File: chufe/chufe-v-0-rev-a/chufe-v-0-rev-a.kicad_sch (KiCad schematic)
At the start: 0 parts

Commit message: agregar borrador
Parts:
- added C1: 100n, symbol Device:C
- added C2: C, symbol Device:C
- added C3: 22u, symbol Device:C_Polarized
- added D1: D, symbol Device:D
- added D2, D3: LED, symbol Device:LED
- added J1: Barrel_Jack_Switch, Connector_BarrelJack:BarrelJack_Horizontal, symbol Connector:Barrel_Jack_Switch
- added R1, R2: 1k, symbol Device:R
- added U1: L7805, symbol Regulator_Linear:L7805
- added U2: URA2412YMD-20WR3_C5369773, easyeda2kicad:PWRM-TH_YLPTEC_VRBXXXXYMD-20WR3, symbol easyeda2kicad:URA2412YMD-20WR3_C5369773
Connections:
- new net: D1.2 (A), D2.2 (A), J1.1
- new net: D3.1 (K), R2.1
- new net: C1.1, D1.1 (K), U1.1 (IN), U2.2 (+VIN)
- new net: D2.1 (K), R1.1
- new net: C2.1, U1.2 (GND)
- new net +12V: U2.3 (+VO1)
- new net +5V: C3.1, D3.2 (A), U1.3 (OUT)
- new net -12V: U2.5 (-VO2)
- new net GND: C1.2, C2.2, C3.2, J1.2, J1.3, R1.2, R2.2, U2.1 (-VIN), U2.4 (COM)
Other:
- company: (none) -> piruetas SpA

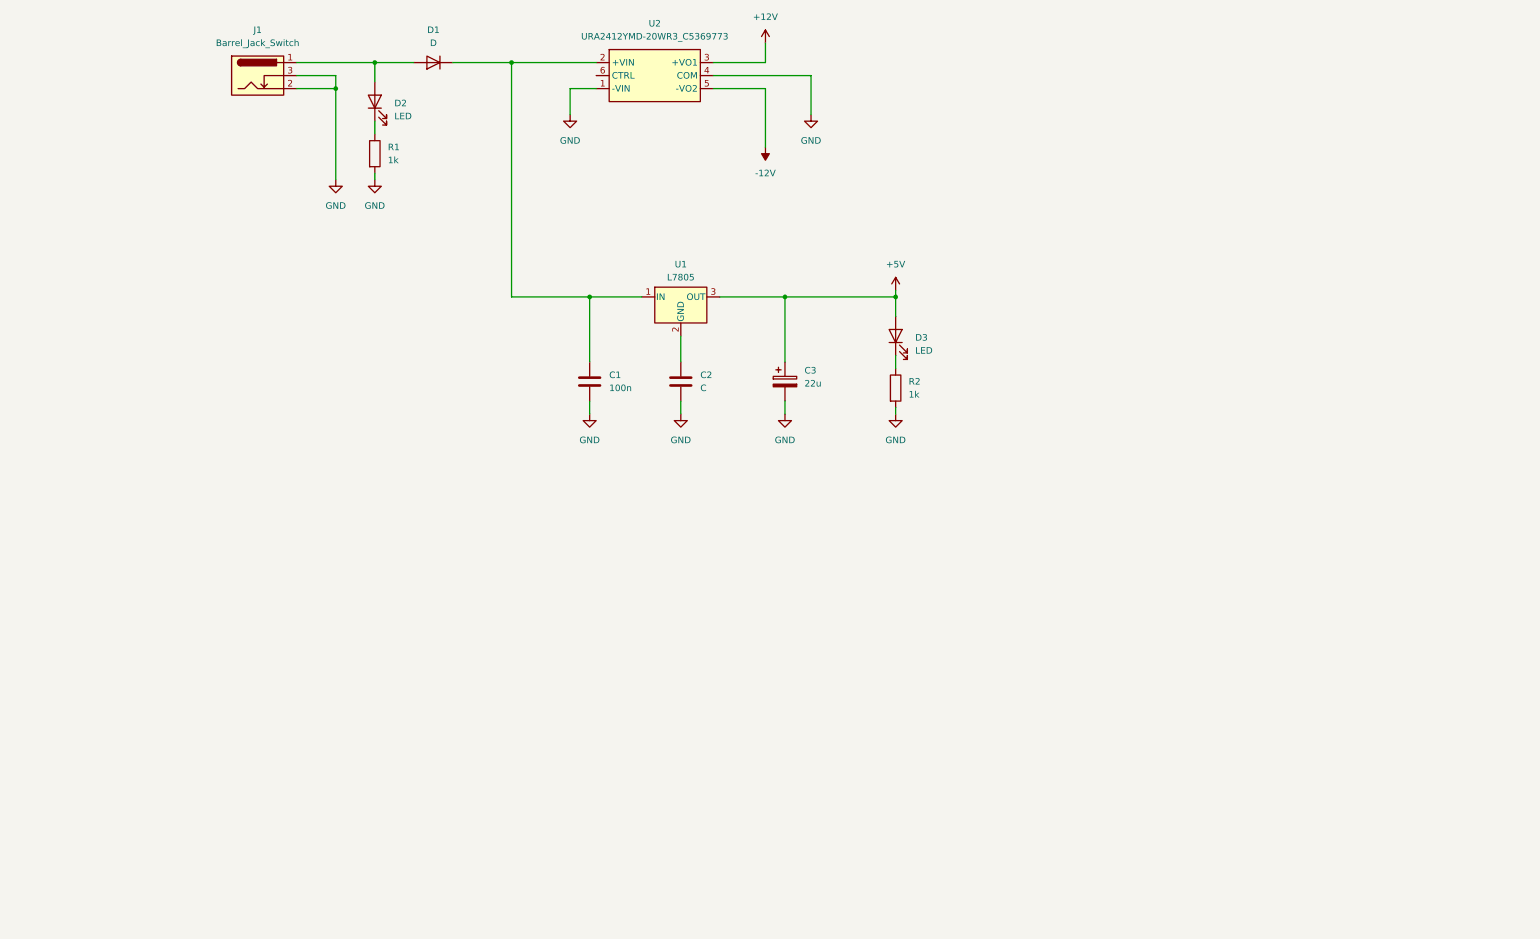
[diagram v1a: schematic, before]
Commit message: agregar ocho conectores
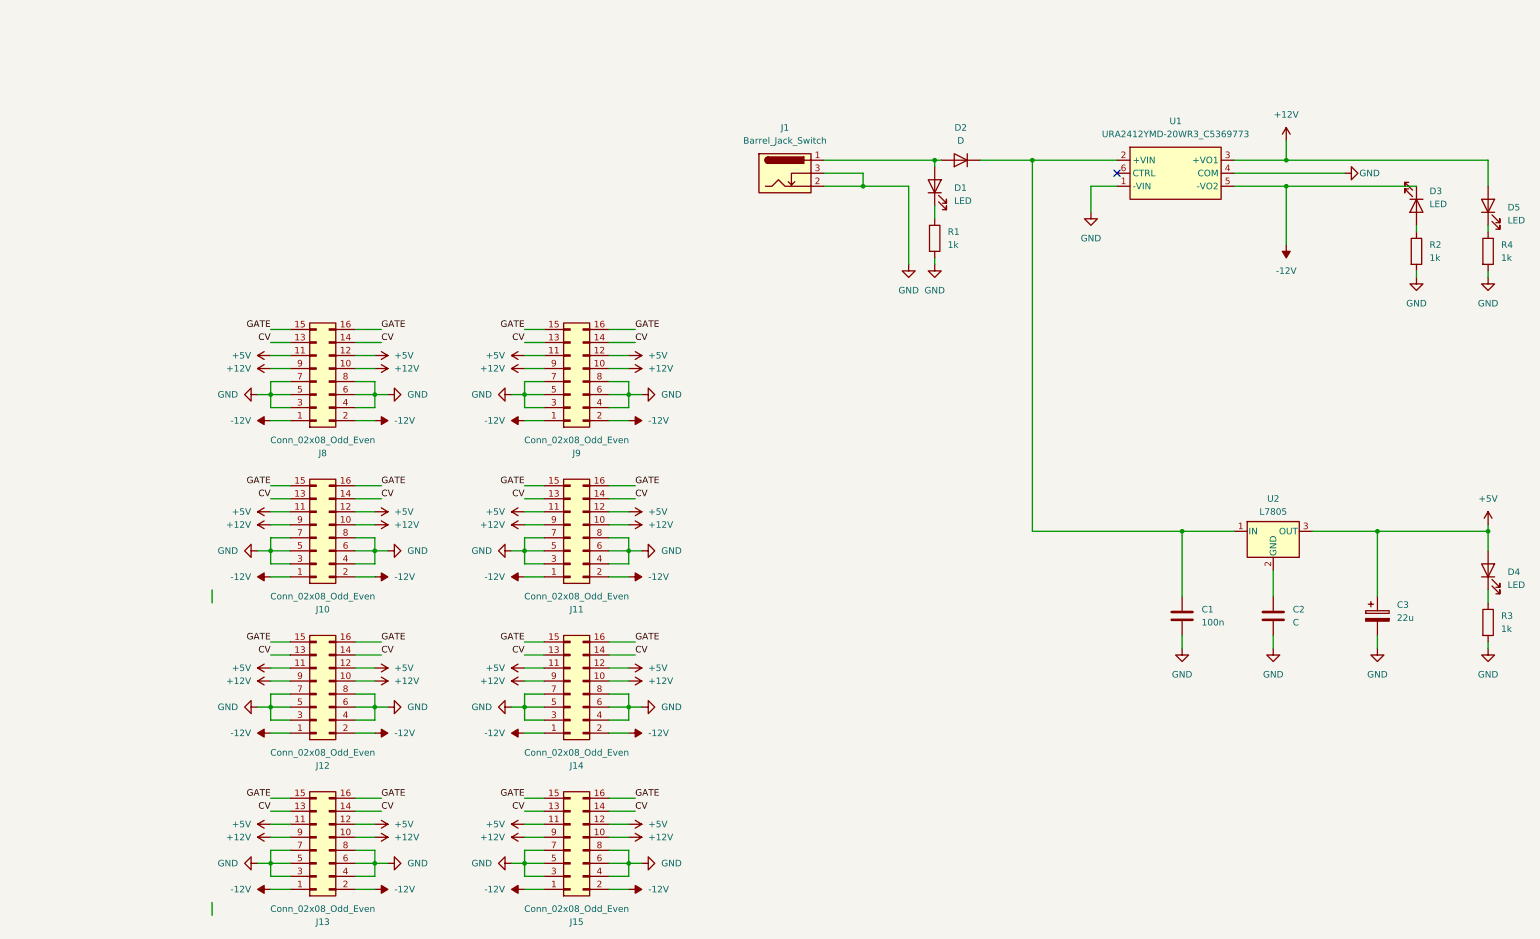
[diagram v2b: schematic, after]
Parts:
- removed D1: D, symbol Device:D
- removed D2: LED, symbol Device:LED
- removed U1: L7805, symbol Regulator_Linear:L7805
- removed U2: URA2412YMD-20WR3_C5369773, easyeda2kicad:PWRM-TH_YLPTEC_VRBXXXXYMD-20WR3, symbol easyeda2kicad:URA2412YMD-20WR3_C5369773
- added D1, D4, D5: LED, symbol Device:LED
- added D2: D, symbol Device:D
- added J10, J11, J12, J13, J14, J15, J8, J9: Conn_02x08_Odd_Even, symbol Connector_Generic:Conn_02x08_Odd_Even
- added R3, R4: 1k, symbol Device:R
- added U1: URA2412YMD-20WR3_C5369773, easyeda2kicad:PWRM-TH_YLPTEC_VRBXXXXYMD-20WR3, symbol easyeda2kicad:URA2412YMD-20WR3_C5369773
- added U2: L7805, symbol Regulator_Linear:L7805
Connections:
- net +12V: now also D5.2 (A), J10.10 (Pin_10), J10.9 (Pin_9), J11.10 (Pin_10), J11.9 (Pin_9), J12.10 (Pin_10), J12.9 (Pin_9), J13.10 (Pin_10), J13.9 (Pin_9), J14.10 (Pin_10), J14.9 (Pin_9), J15.10 (Pin_10), J15.9 (Pin_9), J8.10 (Pin_10), J8.9 (Pin_9), J9.10 (Pin_10), J9.9 (Pin_9), U1.3 (+VO1)
- net +5V: now also D4.2 (A), J10.11 (Pin_11), J10.12 (Pin_12), J11.11 (Pin_11), J11.12 (Pin_12), J12.11 (Pin_11), J12.12 (Pin_12), J13.11 (Pin_11), J13.12 (Pin_12), J14.11 (Pin_11), J14.12 (Pin_12), J15.11 (Pin_11), J15.12 (Pin_12), J8.11 (Pin_11), J8.12 (Pin_12), J9.11 (Pin_11), J9.12 (Pin_12), U2.3 (OUT); no longer D3.2 (A)
- net -12V: now also D3.1 (K), J10.1 (Pin_1), J10.2 (Pin_2), J11.1 (Pin_1), J11.2 (Pin_2), J12.1 (Pin_1), J12.2 (Pin_2), J13.1 (Pin_1), J13.2 (Pin_2), J14.1 (Pin_1), J14.2 (Pin_2), J15.1 (Pin_1), J15.2 (Pin_2), J8.1 (Pin_1), J8.2 (Pin_2), J9.1 (Pin_1), J9.2 (Pin_2), U1.5 (-VO2)
- net GND: now also J10.3 (Pin_3), J10.4 (Pin_4), J10.5 (Pin_5), J10.6 (Pin_6), J10.7 (Pin_7), J10.8 (Pin_8), J11.3 (Pin_3), J11.4 (Pin_4), J11.5 (Pin_5), J11.6 (Pin_6), J11.7 (Pin_7), J11.8 (Pin_8), J12.3 (Pin_3), J12.4 (Pin_4), J12.5 (Pin_5), J12.6 (Pin_6), J12.7 (Pin_7), J12.8 (Pin_8), J13.3 (Pin_3), J13.4 (Pin_4), J13.5 (Pin_5), J13.6 (Pin_6), J13.7 (Pin_7), J13.8 (Pin_8), J14.3 (Pin_3), J14.4 (Pin_4), J14.5 (Pin_5), J14.6 (Pin_6), J14.7 (Pin_7), J14.8 (Pin_8), J15.3 (Pin_3), J15.4 (Pin_4), J15.5 (Pin_5), J15.6 (Pin_6), J15.7 (Pin_7), J15.8 (Pin_8), J8.3 (Pin_3), J8.4 (Pin_4), J8.5 (Pin_5), J8.6 (Pin_6), J8.7 (Pin_7), J8.8 (Pin_8), J9.3 (Pin_3), J9.4 (Pin_4), J9.5 (Pin_5), J9.6 (Pin_6), J9.7 (Pin_7), J9.8 (Pin_8), R3.2, R4.2, U1.1 (-VIN), U1.4 (COM)
- net at J1.1: now also D1.2 (A), D2.2 (A)
- net at R2.1: now also D3.2 (A); no longer D3.1 (K)
- net at C1.1: now also D2.1 (K), U1.2 (+VIN), U2.1 (IN)
- net at R1.1: now also D1.1 (K)
- net at C2.1: now also U2.2 (GND)
- new net: D5.1 (K), R4.1
- new net: D4.1 (K), R3.1
- new net CV: J10.13 (Pin_13), J10.14 (Pin_14), J11.13 (Pin_13), J11.14 (Pin_14), J12.13 (Pin_13), J12.14 (Pin_14), J13.13 (Pin_13), J13.14 (Pin_14), J14.13 (Pin_13), J14.14 (Pin_14), J15.13 (Pin_13), J15.14 (Pin_14), J8.13 (Pin_13), J8.14 (Pin_14), J9.13 (Pin_13), J9.14 (Pin_14)
- new net GATE: J10.15 (Pin_15), J10.16 (Pin_16), J11.15 (Pin_15), J11.16 (Pin_16), J12.15 (Pin_15), J12.16 (Pin_16), J13.15 (Pin_15), J13.16 (Pin_16), J14.15 (Pin_15), J14.16 (Pin_16), J15.15 (Pin_15), J15.16 (Pin_16), J8.15 (Pin_15), J8.16 (Pin_16), J9.15 (Pin_15), J9.16 (Pin_16)
- no-connect marks 0 -> 1
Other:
- title: (none) -> chufe-v-0

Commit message: renombrar
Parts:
- renumbered D5 to D4, D4 to D5, J8 to J1, J10 to J2, J12 to J3, J13 to J4, J9 to J5, J11 to J6, J14 to J7, J15 to J8, J1 to J9, R4 to R3, R3 to R4

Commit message: agregar nueva huella
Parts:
- removed D2: D, symbol Device:D
- added Q1: AO3401A, Package_TO_SOT_SMD:SOT-23, symbol Transistor_FET:Q_PMOS_GSD
- added R5: 1k, Resistor_SMD:R_0805_2012Metric, symbol Device:R
- added R6: 2k2, Resistor_SMD:R_0805_2012Metric, symbol Device:R
- C1: footprint (none) -> Capacitor_SMD:C_0805_2012Metric
- C2: value C -> 100n; footprint (none) -> Capacitor_SMD:C_0805_2012Metric
- C3: footprint (none) -> Capacitor_SMD:CP_Elec_4x5.4
- D1, D3, D4, D5: footprint (none) -> LED_THT:LED_D3.0mm
- J1, J2, J3, J4, J5, J6, J7, J8: footprint (none) -> Connector_IDC:IDC-Header_2x08_P2.54mm_Vertical
- R1, R2, R3: value 1k -> 10k; footprint (none) -> Resistor_SMD:R_0805_2012Metric
- R4: value 1k -> 2k2; footprint (none) -> Resistor_SMD:R_0805_2012Metric
- U2: footprint (none) -> Package_TO_SOT_SMD:TO-252-2
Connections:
- net +12V: now also C1.1, U2.1 (IN)
- net +5V: now also C2.1
- net GND: now also U2.2 (GND), R6.2
- net at J9.1: now also Q1.3 (D); no longer D1.2 (A)
- new net: Q1.1 (G), R5.1, R6.1
- new net: D1.2 (A), Q1.2 (S), R5.2, U1.2 (+VIN)

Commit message: agregar pcb-rev-a
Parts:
- removed J4, J7, J8: Conn_02x08_Odd_Even, Connector_IDC:IDC-Header_2x08_P2.54mm_Vertical, symbol Connector_Generic:Conn_02x08_Odd_Even
- renumbered D3 to D2, D4 to D3, D5 to D4, J5 to J4, J6 to J5, J9 to J6, R6 to R1, R5 to R2, R1 to R3, R2 to R4, R3 to R5, R4 to R6

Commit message: actualizado chufe
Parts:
- removed J2, J3, J4, J5: Conn_02x08_Odd_Even, Connector_IDC:IDC-Header_2x08_P2.54mm_Vertical, symbol Connector_Generic:Conn_02x08_Odd_Even
- removed R2: 1k, Resistor_SMD:R_0805_2012Metric, symbol Device:R
- added D5: BZT52C5V6, symbol Device:D_Zener
- added J4: Conn_01x04_Pin, Connector_Molex:Molex_KK-396_5273-04A_1x04_P3.96mm_Vertical, symbol Connector:Conn_01x04_Pin
- R1: value 2k2 -> 22k; LCSC (none) -> C31850
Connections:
- net +12V: now also J4.4 (Pin_4)
- net +5V: now also J4.3 (Pin_3)
- net -12V: now also J4.1 (Pin_1)
- net GND: now also J4.2 (Pin_2)
- net at Q1.1 (G), R1.1: now also D5.2 (A)
- net at D1.2 (A), Q1.2 (S), U1.2 (+VIN): now also D5.1 (K)
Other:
- moved on the sheet: D1, R3

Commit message: agregar borrador pcb chufe
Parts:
- D1: renamed from D5; footprint (none) -> Diode_SMD:D_SOD-123
- renumbered D1 to D2, D2 to D3, D3 to D4, D4 to D5, J4 to J2, J6 to J3, R3 to R2, R4 to R3, R5 to R4, R6 to R5

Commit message: añadida placa chufe
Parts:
- added H1, H2, H3, H4: M3, MountingHole:MountingHole_3.2mm_M3, symbol Mechanical:MountingHole
